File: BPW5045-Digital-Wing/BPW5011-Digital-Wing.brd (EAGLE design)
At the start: 20.3 x 27.9 mm, 4 parts

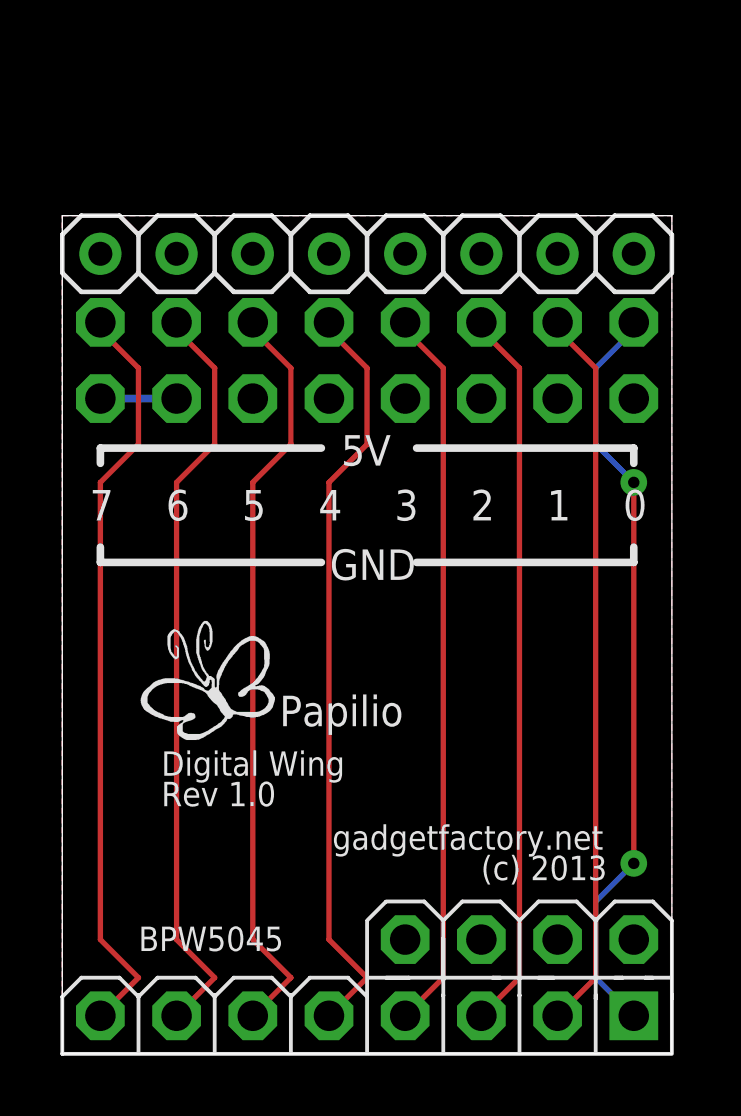
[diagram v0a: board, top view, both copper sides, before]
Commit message: Update Digital Wing to use Grove Connectors
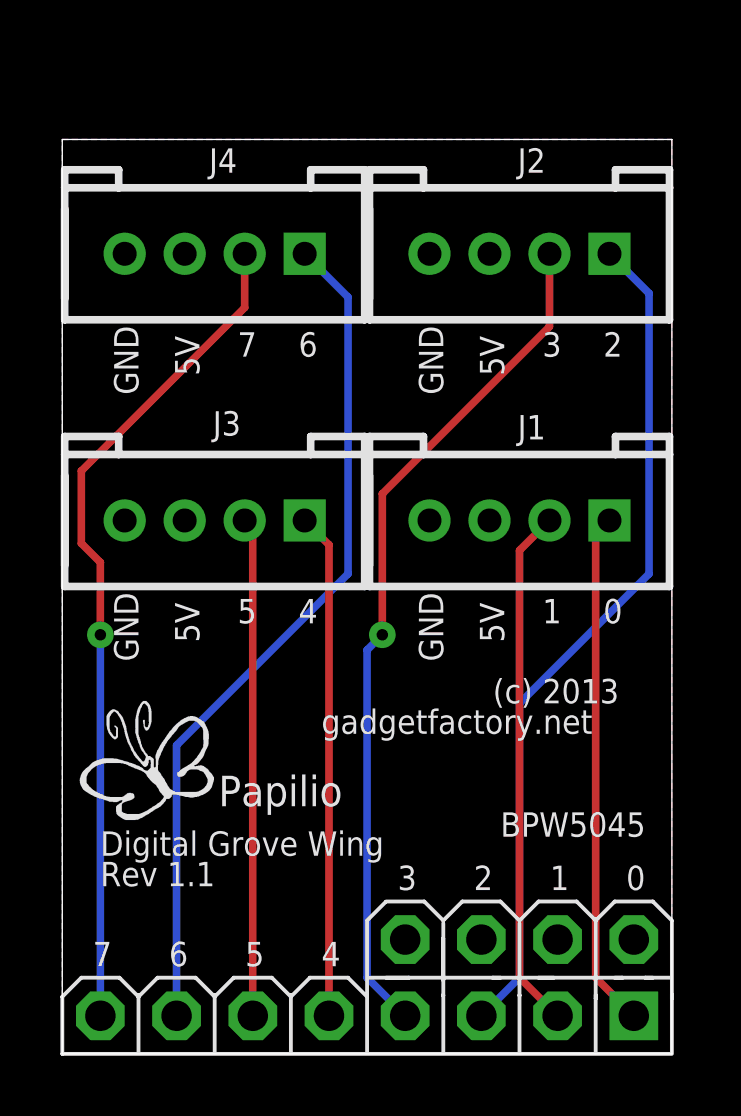
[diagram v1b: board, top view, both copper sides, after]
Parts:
- removed JP1: (no value), GadgetFactory:1X08
- added J1, J3, J4: (no value), GadgetFactory_6.0:CONNECTOR_4P-LEADED-2.0
- J2: device con-lstb:MA08-2 -> GadgetFactory_6.0:CONNECTOR_4P-LEADED-2.0
- moved J2 6.20 mm to (15.2, 26.7)
- moved U$2 3.35 mm to (0.38, 7.24)
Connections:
- net 5V0: now also J1.3, J2.3, J3.3, J4.3; no longer JP1.1, JP1.2, JP1.3, JP1.4, JP1.5, JP1.6, JP1.7, JP1.8
- net GND: now also J1.4, J3.4, J4.4; no longer J2.10, J2.12, J2.14, J2.16, J2.2, J2.6, J2.8
- net N$1: now also J1.1; no longer J2.1
- net N$2: now also J1.2; no longer J2.3
- net N$3: now also J2.1; no longer J2.5
- net N$4: now also J2.2; no longer J2.7
- net N$5: now also J3.1; no longer J2.9
- net N$6: now also J3.2; no longer J2.11
- net N$7: now also J4.1; no longer J2.13
- net N$8: now also J4.2; no longer J2.15
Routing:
- net N$6: track 25.2 -> 16.6 mm
- net N$5: track 25.2 -> 16.8 mm
- net N$1: track 25.2 -> 17.2 mm, vias 2 -> 0
- net N$2: track 24.2 -> 17.5 mm
- net N$4: track 24.2 -> 28.4 mm, vias 0 -> 1
- net N$3: track 24.2 -> 28.3 mm
- net N$7: track 25.2 -> 28.4 mm
- net N$8: track 25.2 -> 27.9 mm, vias 0 -> 1
- net GND: track 2.54 -> 0.00 mm
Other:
- board size 20.3 x 27.9 mm -> 20.3 x 30.5 mm
- board text added: "Digital Grove Wing"
- board text added: "Rev 1.1"
- board text removed: "Digital Wing"
- board text removed: "Rev 1.0"

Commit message: Add 5V resistors for Digital Grove Wing
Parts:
- added R1, R2, R3, R4, R5, R6, R7, R8: 390, GadgetFactory:0805
- moved U$2 7.19 mm to (6.22, 11.4)
- moved J1 2.54 mm to (15.2, 20.3)
- moved J2 2.54 mm to (15.2, 29.2)
- moved J3 2.54 mm to (5.08, 20.3)
- moved J4 2.54 mm to (5.08, 29.2)
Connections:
- new net N$10: R2.1, U$1.6
- new net N$11: R3.1, U$1.5
- new net N$12: R4.1, U$1.4
- new net N$13: R5.1, U$1.3
- new net N$14: R6.1, U$1.2
- new net N$15: R7.1, U$1.1
- new net N$16: R8.1, U$1.0
- new net N$9: R1.1, U$1.7
- net N$1: now also R8.2; no longer U$1.0
- net N$2: now also R7.2; no longer U$1.1
- net N$3: now also R6.2; no longer U$1.2
- net N$4: now also R5.2; no longer U$1.3
- net N$5: now also R4.2; no longer U$1.4
- net N$6: now also R3.2; no longer U$1.5
- net N$7: now also R2.2; no longer U$1.6
- net N$8: now also R1.2; no longer U$1.7
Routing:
- net 5V0: track 0.00 -> 12.0 mm, vias 0 -> 1
- net N$15: track 0.00 -> 7.16 mm
- net N$14: track 0.00 -> 7.16 mm
- net N$16: track 0.00 -> 7.16 mm
- net N$13: track 0.00 -> 7.16 mm
- net N$2: track 17.5 -> 11.0 mm
- net N$4: track 28.4 -> 22.5 mm, vias 1 -> 0
- net N$1: track 17.2 -> 11.3 mm
- net N$3: track 28.3 -> 23.3 mm, vias 0 -> 1
- net N$9: track 0.00 -> 3.70 mm
- net N$12: track 0.00 -> 3.70 mm
- net N$11: track 0.00 -> 3.70 mm
- net N$10: track 0.00 -> 3.70 mm
- net N$8: track 27.9 -> 24.8 mm, vias 1 -> 0
- net N$7: track 28.4 -> 25.2 mm, vias 0 -> 1
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- added copper zone on layer 1, net 5V0
- added copper zone on layer 16, net GND
- removed copper zone on layer 16, net 5V0
- removed copper zone on layer 1, net GND
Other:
- board size 20.3 x 30.5 mm -> 20.3 x 33 mm
- board text added: "Rev 1.2"
- board text removed: "(c) 2013"
- board text removed: "Rev 1.1"
- board text removed: "gadgetfactory.net"
